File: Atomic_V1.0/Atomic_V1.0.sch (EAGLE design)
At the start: 10 parts, among them U4 TLE9250VSJ, X1 S4P-VH

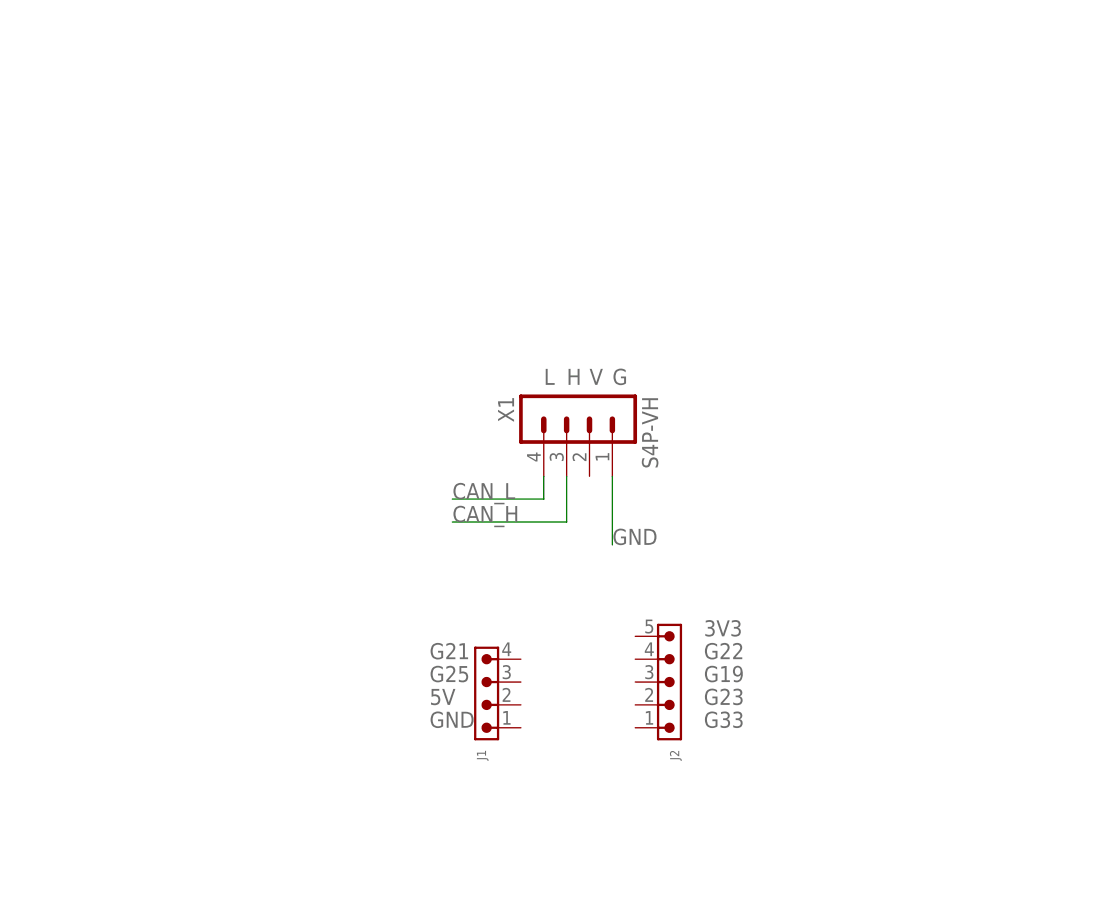
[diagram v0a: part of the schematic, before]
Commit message: 2 Airwires
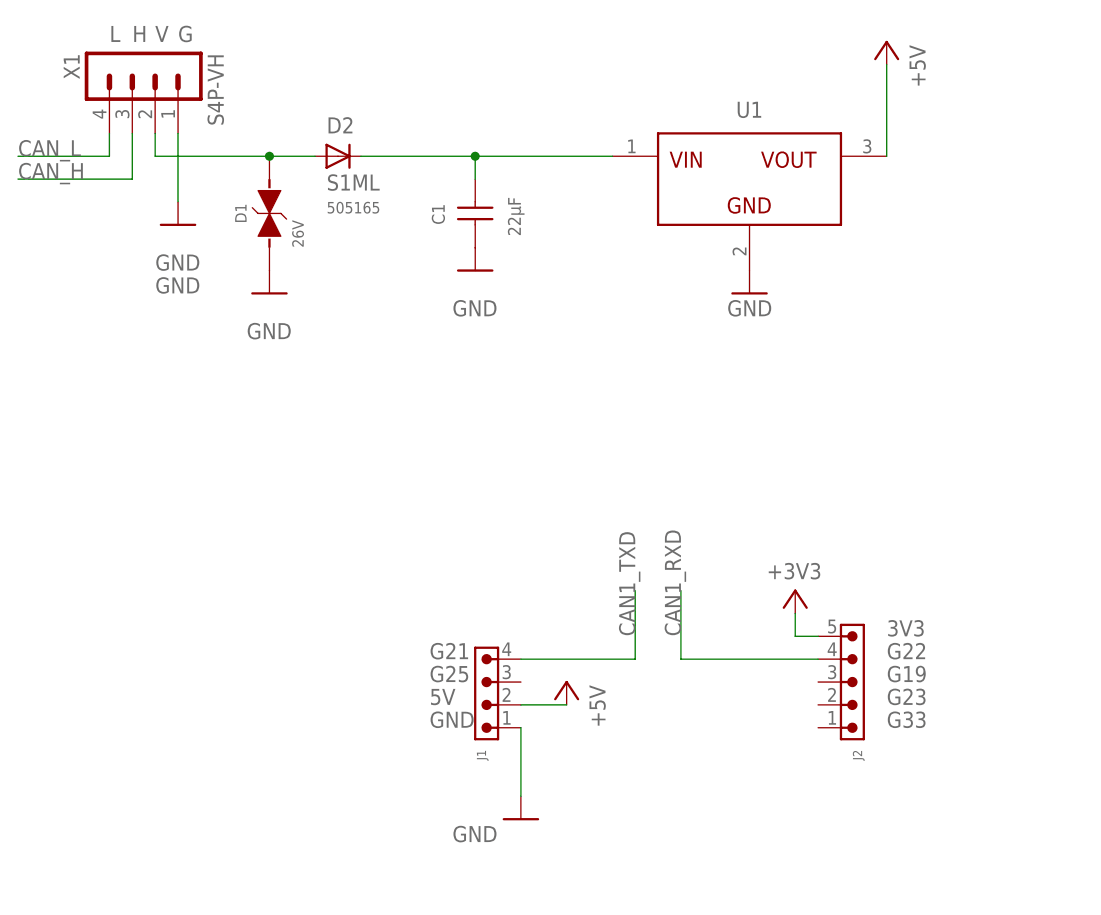
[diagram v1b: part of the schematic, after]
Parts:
- added C1: 22µF, Wurth_Capacitors_WCAP-CSGP:WCAP-CSGP_1210_H2.5_885012109014_25V(DC)
- added D1: 26V, Wurth_EMC Components_WE-TVSP:WE-TVSP_DO-214AC_400W_BI_824501261
- added D2: S1ML, fliegl-elektronik:S1ML
- added U1: (no value), Wurth_Step Down Converter_MagI³C-FDSM:MAGI³C-FDSM_SIP-3_173010542_173XXXX42
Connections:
- new net +12V: D1.2, D2.A, X1.2
- new net N$1: C1.2, D2.C, U1.VIN
- net +3V3: now also J2.5
- net +5V: now also J1.2, U1.VOUT
- net CAN1_RXD: now also J2.4
- net CAN1_TXD: now also J1.4
- net GND: now also C1.1, D1.1, J1.1, U1.GND
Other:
- moved on the sheet: J2, X1

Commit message: collission avoid.
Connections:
- net CAN_H renamed CAN_P
- net CAN_L renamed CAN_N
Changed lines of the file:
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@@
 <setting verticaltext="up"/>
 </settings>
-<grid distance="0.1" unitdist="inch" unit="inch" style="lines" multiple="1" display="yes" altdistance="0.01" altunitdist="inch" altunit="inch"/>
+<grid distance="0.1" unitdist="inch" unit="inch" style="lines" multiple="1" display="no" altdistance="0.01" altunitdist="inch" altunit="inch"/>
 <layers>
 <layer number="1" name="Top" color="4" fill="1" visible="no" active="no"/>
@@
 </segment>
 </net>
-<net name="CAN_H" class="0">
+<net name="CAN_P" class="0">
 <segment>
 <wire x1="149.86" y1="81.28" x2="149.86" y2="91.44" width="0.1524" layer="91"/>
@@
 </segment>
 </net>
-<net name="CAN_L" class="0">
+<net name="CAN_N" class="0">
 <segment>
 <wire x1="149.86" y1="76.2" x2="149.86" y2="66.04" width="0.1524" layer="91"/>

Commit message: made PDF
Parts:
- C1: value 22µF -> 47uF
- D2: value S1ML -> SS12L R3
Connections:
- net CAN_N renamed CAN_L
- net CAN_P renamed CAN_H

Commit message: DCDC Version
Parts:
- removed D2: SS12L R3, fliegl-elektronik:S1ML
- added D3: SS12L_R3, SS12L_R3:SS12L_R3
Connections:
- net +12V: now also D3.A; no longer D2.A
- net N$1: now also D3.K; no longer D2.C
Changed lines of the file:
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@@
 <part name="P+3" library="supply1" deviceset="+5V" device=""/>
 <part name="D1" library="Wurth_EMC Components_WE-TVSP" library_urn="urn:adsk.eagle:library:14283044" deviceset="WE-TVSP_DO-214AC_400W_BI" device="" package3d_urn="urn:adsk.eagle:package:12146531/2" technology="_824501261" value="26V"/>
-<part name="D2" library="fliegl-elektronik" deviceset="S1ML" device="" value="SS12L R3"/>
 <part name="GND4" library="supply1" deviceset="GND" device=""/>
 <part name="C1" library="Wurth_Capacitors_WCAP-CSGP" library_urn="urn:adsk.eagle:library:18488985" deviceset="WCAP-CSGP_1210_H2.5" device="_25V(DC)" package3d_urn="urn:adsk.eagle:package:18489097/2" technology="_885012109014" value="47uF"/>
 <part name="GND6" library="supply1" deviceset="GND" device=""/>
+<part name="D3" library="SS12L_R3" deviceset="SS12L_R3" device=""/>
 </parts>
 <sheets>
@@
 <attribute name="VALUE" x="-11.43" y="116.84" size="1.27" layer="95" rot="R90"/>
 </instance>
-<instance part="D2" gate="G$1" x="-7.62" y="127" smashed="yes">
-<attribute name="NAME" x="-8.89" y="129.54" size="1.778" layer="95"/>
-<attribute name="VALUE" x="-8.89" y="123.19" size="1.778" layer="96"/>
-<attribute name="ARTIKEL_NR" x="-8.89" y="120.65" size="1.27" layer="96"/>
-</instance>
 <instance part="GND4" gate="1" x="-15.24" y="111.76" smashed="yes">
 <attribute name="VALUE" x="-17.78" y="106.68" size="1.778" layer="96"/>
@@
 <instance part="GND6" gate="1" x="7.62" y="114.3" smashed="yes">
 <attribute name="VALUE" x="5.08" y="109.22" size="1.778" layer="96"/>
+</instance>
+<instance part="D3" gate="G$1" x="5.08" y="127" smashed="yes" rot="R180">
+<attribute name="NAME" x="1.27" y="139.7" size="1.778" layer="95" rot="R180" align="center-left"/>
+<attribute name="VALUE" x="1.27" y="134.62" size="1.778" layer="96" rot="R180" align="center-left"/>
 </instance>
 </instances>
@@
 <pinref part="X1" gate="G$1" pin="2"/>
 <wire x1="-27.94" y1="129.54" x2="-27.94" y2="127" width="0.1524" layer="91"/>
-<pinref part="D2" gate="G$1" pin="A"/>
+<pinref part="D1" gate="G$1" pin="2"/>
 <wire x1="-10.16" y1="127" x2="-15.24" y2="127" width="0.1524" layer="91"/>
-<pinref part="D1" gate="G$1" pin="2"/>
 <wire x1="-15.24" y1="127" x2="-27.94" y2="127" width="0.1524" layer="91"/>
 <junction x="-15.24" y="127"/>
+<pinref part="D3" gate="G$1" pin="A"/>
 </segment>
 </net>
@@
 <segment>
 <pinref part="U1" gate="G$1" pin="VIN"/>
-<pinref part="D2" gate="G$1" pin="C"/>
-<wire x1="-5.08" y1="127" x2="7.62" y2="127" width="0.1524" layer="91"/>
 <pinref part="C1" gate="G$1" pin="2"/>
+<wire x1="5.08" y1="127" x2="7.62" y2="127" width="0.1524" layer="91"/>
 <wire x1="7.62" y1="127" x2="22.86" y2="127" width="0.1524" layer="91"/>
 <wire x1="7.62" y1="124.46" x2="7.62" y2="127" width="0.1524" layer="91"/>
 <junction x="7.62" y="127"/>
+<pinref part="D3" gate="G$1" pin="K"/>
 </segment>
 </net>
